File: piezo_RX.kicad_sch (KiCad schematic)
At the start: 5 parts, among them J3 1053091102

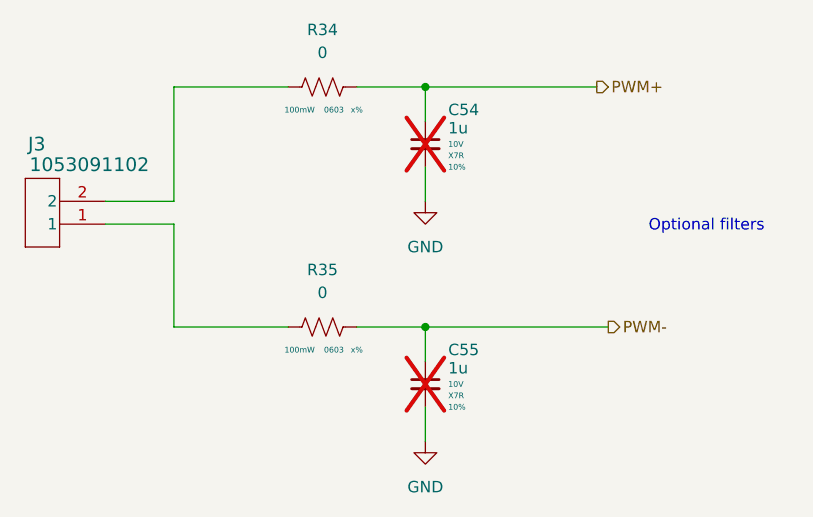
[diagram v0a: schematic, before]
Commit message: Made most capacitors 0402 for mcu sheets, defined board shape and started layout
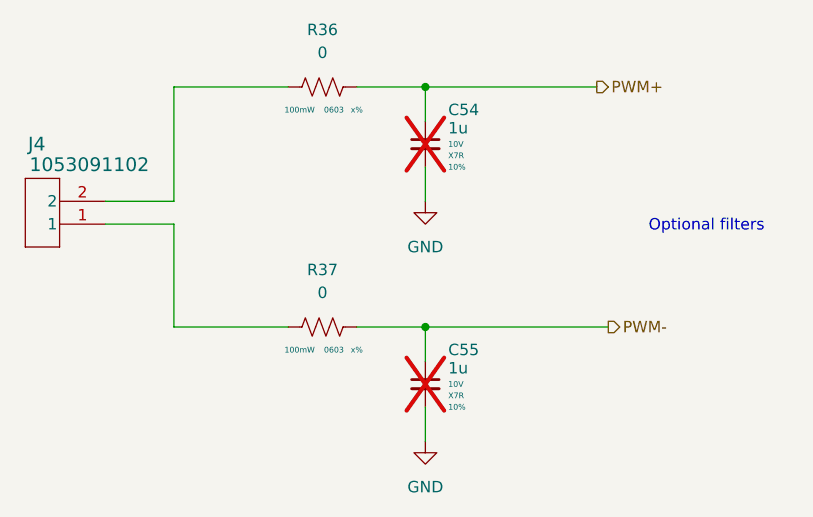
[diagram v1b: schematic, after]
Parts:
- renumbered J3 to J4, R34 to R36, R35 to R37
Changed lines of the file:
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@@
 		(dnp no)
 		(fields_autoplaced yes)
-		(property "Reference" "#PWR065"
+		(property "Reference" "#PWR068"
 			(at 153.67 128.27 0)
 			(hide yes)
@@
 			(project "Temp-Logger"
 				(path "/9c5f4d5b-9930-4cae-a7d7-03685cadac72/8722ad6e-d449-40f5-b9d3-e719432ce7be/e89cf95b-fb60-44a5-9f2e-e0e3227c6da9"
-					(reference "#PWR065")
+					(reference "#PWR068")
 					(unit 1)
 				)
@@
 		(dnp no)
 		(fields_autoplaced yes)
-		(property "Reference" "R35"
+		(property "Reference" "R37"
 			(at 142.24 102.87 0)
 			(show_name no)
@@
 			(project "Temp-Logger"
 				(path "/9c5f4d5b-9930-4cae-a7d7-03685cadac72/8722ad6e-d449-40f5-b9d3-e719432ce7be/e89cf95b-fb60-44a5-9f2e-e0e3227c6da9"
-					(reference "R35")
+					(reference "R37")
 					(unit 1)
 				)
@@
 		(in_pos_files yes)
 		(dnp no)
-		(property "Reference" "J3"
+		(property "Reference" "J4"
 			(at 110.49 88.9 0)
 			(show_name no)
@@
 			(project "Temp-Logger"
 				(path "/9c5f4d5b-9930-4cae-a7d7-03685cadac72/8722ad6e-d449-40f5-b9d3-e719432ce7be/e89cf95b-fb60-44a5-9f2e-e0e3227c6da9"
-					(reference "J3")
+					(reference "J4")
 					(unit 1)
 				)
@@
 		(dnp no)
 		(fields_autoplaced yes)
-		(property "Reference" "R34"
+		(property "Reference" "R36"
 			(at 142.24 76.2 0)
 			(show_name no)
@@
 			(project "Temp-Logger"
 				(path "/9c5f4d5b-9930-4cae-a7d7-03685cadac72/8722ad6e-d449-40f5-b9d3-e719432ce7be/e89cf95b-fb60-44a5-9f2e-e0e3227c6da9"
-					(reference "R34")
+					(reference "R36")
 					(unit 1)
 				)
@@
 		(dnp no)
 		(fields_autoplaced yes)
-		(property "Reference" "#PWR064"
+		(property "Reference" "#PWR067"
 			(at 153.67 101.6 0)
 			(hide yes)
@@
 			(project "Temp-Logger"
 				(path "/9c5f4d5b-9930-4cae-a7d7-03685cadac72/8722ad6e-d449-40f5-b9d3-e719432ce7be/e89cf95b-fb60-44a5-9f2e-e0e3227c6da9"
-					(reference "#PWR064")
+					(reference "#PWR067")
 					(unit 1)
 				)
